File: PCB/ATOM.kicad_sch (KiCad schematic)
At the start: 0 parts

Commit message: upload symbol
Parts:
- added D1, D10, D11, D12, D13, D14, D15, D16, D17, D18, D19, D2, D20, D21, D3, D4, D5, D6, D7, D8, D9: BAV70, ATOM:SOT-23, symbol atom:BAV70
- added SW1, SW10, SW11, SW12, SW13, SW14, SW15, SW16, SW17, SW18, SW19, SW2, SW20, SW21, SW22, SW23, SW24, SW25, SW26, SW27, SW28, SW29, SW3, SW30, SW31, SW32, SW33, SW34, SW35, SW36, SW37, SW38, SW39, SW4, SW40, SW41, SW42, SW5, SW6, SW7, SW8, SW9: SW_Push, ATOM:SW_Hotswap_Kailh_CPG1353, symbol atom:SW_Push
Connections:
- new net: D9.2 (A), SW18.1
- new net: D1.2 (A), SW2.1
- new net: D18.2 (A), SW36.1
- new net: D10.1 (A), SW19.2
- new net: D15.2 (A), SW30.1
- new net: D6.2 (A), SW12.1
- new net: D9.1 (A), SW17.2
- new net: D13.2 (A), SW26.1
- new net: D17.1 (A), SW33.2
- new net: D17.2 (A), SW34.1
- new net: D20.2 (A), SW40.1
- new net: D12.1 (A), SW23.2
- new net: D12.2 (A), SW24.1
- new net: D2.1 (A), SW3.2
- new net: D8.2 (A), SW16.1
- new net: D3.2 (A), SW6.1
- new net: D5.2 (A), SW10.1
- new net: D14.2 (A), SW28.1
- new net: D14.1 (A), SW27.2
- new net: D2.2 (A), SW4.1
- new net: D16.2 (A), SW32.1
- new net: D16.1 (A), SW31.2
- new net: D3.1 (A), SW5.2
- new net: D8.1 (A), SW15.2
- new net: D6.1 (A), SW11.2
- new net: D7.1 (A), SW13.2
- new net: D7.2 (A), SW14.1
- new net: D13.1 (A), SW25.2
- new net: D4.2 (A), SW8.1
- new net: D11.2 (A), SW22.1
- new net: D18.1 (A), SW35.2
- new net: D1.1 (A), SW1.2
- new net: D19.2 (A), SW38.1
- new net: D4.1 (A), SW7.2
- new net: D19.1 (A), SW37.2
- new net: D5.1 (A), SW9.2
- new net: D21.2 (A), SW42.1
- new net: D21.1 (A), SW41.2
- new net: D10.2 (A), SW20.1
- new net: D15.1 (A), SW29.2
- new net: D11.1 (A), SW21.2
- new net: D20.1 (A), SW39.2
- new net COL0: SW1.1, SW13.1, SW25.1
- new net COL1: SW14.2, SW2.2, SW26.2
- new net COL10: SW11.1
- new net COL11: SW12.2, SW24.2, SW36.2
- new net COL2: SW15.1, SW27.1, SW3.1
- new net COL3: SW4.2
- new net COL4: SW17.1, SW29.1, SW37.1, SW5.1
- new net COL5: SW18.2, SW30.2, SW38.2, SW6.2
- new net COL6: SW19.1, SW31.1, SW39.1, SW7.1
- new net COL7: SW20.2, SW32.2, SW40.2, SW8.2
- new net COL8: SW21.1, SW33.1, SW41.1, SW9.1
- new net COL9: SW10.2, SW22.2, SW34.2, SW42.2
- new net ROW0: D1.3 (K), D2.3 (K), D3.3 (K), D4.3 (K), D5.3 (K), D6.3 (K)
- new net ROW1: D10.3 (K), D11.3 (K), D12.3 (K), D7.3 (K), D8.3 (K), D9.3 (K)
- new net ROW2: D13.3 (K), D14.3 (K), D15.3 (K), D16.3 (K), D17.3 (K), D18.3 (K)
- new net ROW3: D19.3 (K), D20.3 (K), D21.3 (K)

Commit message: route matrix
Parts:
- added C1: 100nF, symbol atom:C_Small
- added F1: 500mA, symbol atom:Polyfuse_Small
- added J1: USB_C_Receptacle_USB2.0_16P, symbol atom:USB_C_Receptacle_USB2.0_16P
- added R1, R2: 5.1K, symbol atom:R_Small
- added R3: 1M, symbol atom:R_Small
- added U1: E73-2G4M08S1C-52840, ATOM:E73-2G4M08S1C-52840, symbol atom:E73-2G4M08S1C-52840
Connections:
- net COL10: now also SW23.1, SW35.1
- net COL3: now also SW16.2, SW28.2, SW37.1
- net COL4: now also SW38.2; no longer SW37.1
- net COL5: now also SW39.1, U1.12 (P0.26); no longer SW38.2
- net COL6: now also SW40.2, U1.22 (P0.07); no longer SW39.1
- net COL7: now also SW41.1; no longer SW40.2
- net COL8: now also SW42.2; no longer SW41.1
- net COL9: no longer SW42.2
- new net: F1.1, J1.A4 (VBUS), J1.A9 (VBUS), J1.B4 (VBUS), J1.B9 (VBUS)
- new net: J1.B5 (CC2), R2.1
- new net: J1.A5 (CC1), R1.1
- new net GND: C1.1, C1.2, J1.A1 (GND), J1.A12 (GND), J1.B1 (GND), J1.B12 (GND), J1.S1 (SHIELD), R1.2, R2.2, R3.1, R3.2, U1.21 (GND), U1.24 (GND), U1.5 (GND)
- new net USBM: J1.A7 (D-), J1.B7 (D-)
- new net USBP: J1.A6 (D+), J1.B6 (D+)
- new net VBUS: F1.2
- no-connect marks 0 -> 2
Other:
- moved on the sheet: D19, D20, D21, SW37, SW38, SW39, SW40, SW41, SW42

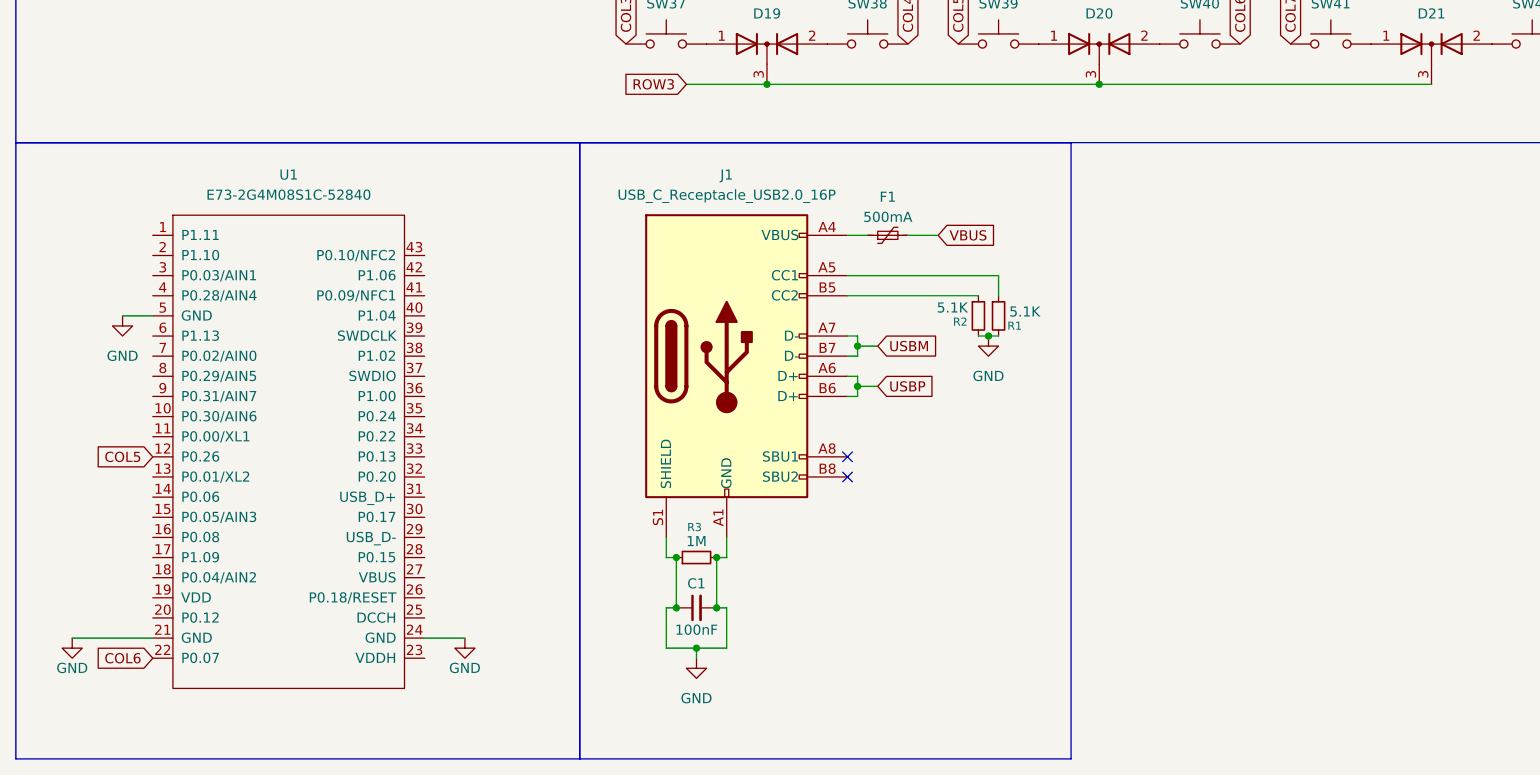
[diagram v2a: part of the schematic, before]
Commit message: route daughterboard
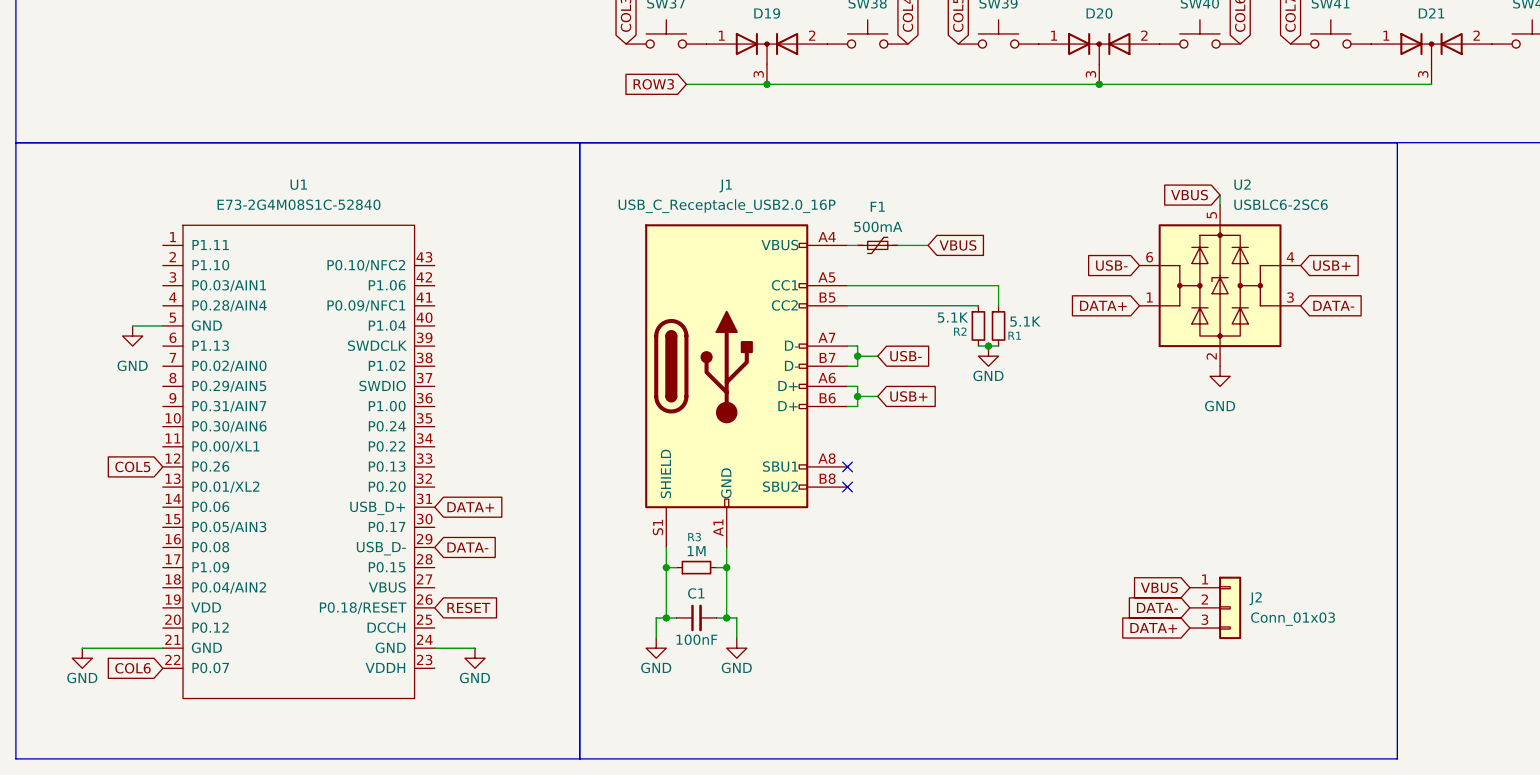
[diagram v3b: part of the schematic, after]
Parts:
- added J2: Conn_01x03, ATOM:JST_PH_S3B-PH-SM4-TB_1x03-1MP_P2.00mm_Horizontal, symbol atom:Conn_01x03
- added U2: USBLC6-2SC6, ATOM:TSOT-23-6_HandSoldering, symbol atom:USBLC6-2SC6
- C1: footprint (none) -> ATOM:C_0603_1608Metric_Pad1.08x0.95mm_HandSolder
- F1: footprint (none) -> ATOM:Fuse_1206_3216Metric_Pad1.42x1.75mm_HandSolder
- J1: footprint (none) -> ATOM:USB_C_Receptacle_HRO_TYPE-C-31-M-12
- R1, R2, R3: footprint (none) -> ATOM:R_0603_1608Metric_Pad0.98x0.95mm_HandSolder
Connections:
- net GND: now also U2.2 (GND)
- net VBUS: now also J2.1 (Pin_1), U2.5 (VBUS)
- net RESET: now reaches U1.26 (P0.18/RESET)
- net DATA-: now reaches U1.29 (USB_D-)
- net DATA-: now also J2.2 (Pin_2), U2.3 (I/O2)
- net DATA+: now reaches U1.31 (USB_D+)
- net DATA+: now also J2.3 (Pin_3), U2.1 (I/O1)
- net USBM renamed USB-
- net USB-: now also U2.6 (I/O1)
- net USBP renamed USB+
- net USB+: now also U2.4 (I/O2)
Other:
- moved on the sheet: C1, F1, J1, R1, R2, R3, U1
